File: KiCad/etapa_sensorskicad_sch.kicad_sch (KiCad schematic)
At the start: 9 parts, among them J5 Conn_01x04_Pin, U23 FXTH87, U6 FDC2214

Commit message: Correccions dels sheets i títols fetes
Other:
- title: (none) -> Etapa de Sensors del projecte
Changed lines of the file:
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@@
 	(generator_version "9.0")
 	(paper "A4")
+	(title_block
+		(title "Etapa de Sensors del projecte")
+	)
 	(text "FXTH87 \n(Pressió)"
 		(exclude_from_sim no)

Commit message: ALFRED DEGANOS SECOOOOS PLS DADDY ALFRED TE CAMELAMOS
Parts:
- removed C32, C33: 100nF, Capacitor_SMD:C_0805_2012Metric, symbol Device:C
- removed FB2: FerriteBead, Inductor_SMD:L_1812_4532Metric, symbol Device:FerriteBead
- removed J5: Conn_01x04_Pin, Connector_PinHeader_2.54mm:PinHeader_1x04_P2.54mm_Vertical, symbol Connector:Conn_01x04_Pin
- removed R5: 10k, Resistor_SMD:R_0805_2012Metric, symbol Device:R
- removed U23: FXTH87, Package_DFN_QFN:UDC-QFN-20-4EP_3x4mm_P0.5mm_EP0.41x0.25mm, symbol FXTH87:FXTH87
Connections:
- no-connect marks 21 -> 7
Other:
- note removed: "FXTH87 (Pressió)"
- note removed: "Programador de Sensor de Pressió"
- note removed: "Programar sensor per rebre enviar senyals PWM"

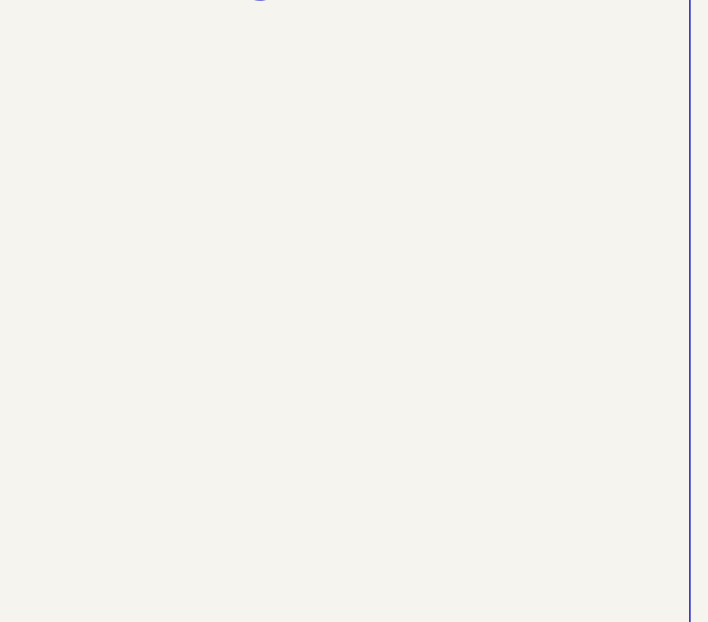
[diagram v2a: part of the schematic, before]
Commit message: Routing de l'alimentació fet, s'ha afegit connector del mòdul RF i plànols millorats
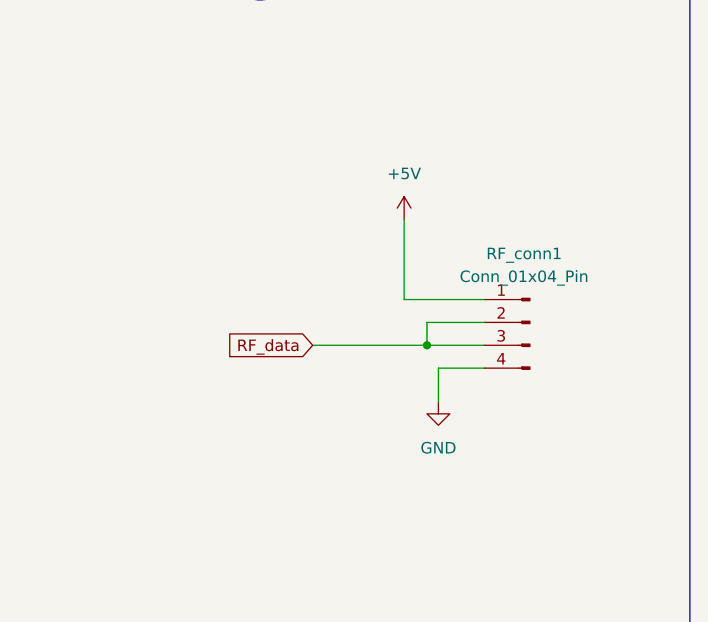
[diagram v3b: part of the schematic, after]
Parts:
- added RF_conn1: Conn_01x04_Pin, Connector_PinSocket_2.54mm:PinSocket_1x04_P2.54mm_Vertical, symbol Connector:Conn_01x04_Pin
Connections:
- net GND: now also RF_conn1.4 (Pin_4)
- new net +5V: RF_conn1.1 (Pin_1)
- new net RF_data: RF_conn1.2 (Pin_2), RF_conn1.3 (Pin_3)

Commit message: Nose broderk
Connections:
- net RF_data renamed RF_data0
- net RF_data0: no longer RF_conn1.2 (Pin_2)
- new net RF_data1: RF_conn1.2 (Pin_2)
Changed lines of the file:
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@@
 		(color 0 0 0 0)
 	)
-	(junction
-		(at 144.78 63.5)
-		(diameter 0)
-		(color 0 0 0 0)
-	)
 	(no_connect
 		(at 31.75 64.77)
@@
 	(wire
 		(pts
-			(xy 144.78 60.96) (xy 144.78 63.5)
-		)
-		(stroke
-			(width 0)
-			(type default)
-		)
-	)
-	(wire
-		(pts
 			(xy 146.05 66.04) (xy 146.05 69.85)
 		)
@@
 	(wire
 		(pts
+			(xy 130.81 60.96) (xy 151.13 60.96)
+		)
+		(stroke
+			(width 0)
+			(type default)
+		)
+	)
+	(wire
+		(pts
 			(xy 31.75 68.58) (xy 24.13 68.58)
 		)
@@
 	(wire
 		(pts
-			(xy 132.08 63.5) (xy 144.78 63.5)
+			(xy 130.81 63.5) (xy 151.13 63.5)
 		)
 		(stroke
@@
 	(wire
 		(pts
-			(xy 151.13 60.96) (xy 144.78 60.96)
-		)
-		(stroke
-			(width 0)
-			(type default)
-		)
-	)
-	(wire
-		(pts
 			(xy 31.75 57.15) (xy 24.13 57.15)
 		)
@@
 		(pts
 			(xy 19.05 74.93) (xy 31.75 74.93)
-		)
-		(stroke
-			(width 0)
-			(type default)
-		)
-	)
-	(wire
-		(pts
-			(xy 144.78 63.5) (xy 151.13 63.5)
 		)
 		(stroke
@@
 		)
 	)
+	(global_label "RF_data1"
+		(shape output)
+		(at 130.81 60.96 180)
+		(fields_autoplaced yes)
+		(effects
+			(font
+				(size 1.27 1.27)
+			)
+			(justify right)
+		)
+		(property "Intersheetrefs" "${INTERSHEET_REFS}"
+			(at 119.1164 60.96 0)
+			(effects
+				(font
+					(size 1.27 1.27)
+				)
+				(justify right)
+				(hide yes)
+			)
+		)
+	)
 	(global_label "SDA"
 		(shape bidirectional)
@@
 		)
 	)
-	(global_label "RF_data"
-		(shape input)
-		(at 132.08 63.5 180)
+	(global_label "RF_data0"
+		(shape output)
+		(at 130.81 63.5 180)
 		(fields_autoplaced yes)
 		(effects
@@
 		)
 		(property "Intersheetrefs" "${INTERSHEET_REFS}"
-			(at 121.5959 63.5 0)
+			(at 119.1164 63.5 0)
 			(effects
 				(font

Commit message: Coses vàries nose
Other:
- note added: "Sensor i Mòdul RF (connector)"
- note removed: "Sensors amb connectors genèrics"
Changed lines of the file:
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@@
 		(title "Etapa de Sensors del projecte")
 	)
-	(text "Sensors amb connectors genèrics"
+	(text "Sensor i Mòdul RF (connector)"
 		(exclude_from_sim no)
 		(at 91.44 21.59 0)
